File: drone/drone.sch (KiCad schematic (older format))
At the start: 16 parts

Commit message: Worked on the drone
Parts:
- X1: renamed from X?; value CRYSTAL -> 12MHz
- gave numbers to parts that had none: 15
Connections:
- no-connect marks 0 -> 9
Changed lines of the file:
@@
 $EndDescr
 $Comp
-L CRYSTAL X?
+L CRYSTAL X1
 U 1 1 556BC952
 P 1575 1875
-F 0 "X?" H 1575 2025 60  0000 C CNN
-F 1 "CRYSTAL" H 1575 1725 60  0000 C CNN
+F 0 "X1" H 1575 2025 60  0000 C CNN
+F 1 "12MHz" H 1575 1725 60  0000 C CNN
 F 2 "" H 1575 1875 60  0000 C CNN
 F 3 "" H 1575 1875 60  0000 C CNN
@@
 $EndComp
 $Comp
-L AT89S4051-P IC?
+L AT89S4051-P IC1
 U 1 1 556CD57A
 P 3125 2175
-F 0 "IC?" H 2175 3175 40  0000 C CNN
+F 0 "IC1" H 2175 3175 40  0000 C CNN
 F 1 "AT89S4051-P" H 3875 1275 40  0000 C CNN
 F 2 "DIP20" H 3125 2175 30  0000 C CIN
@@
 $EndComp
 $Comp
-L RELAY_2RT K?
+L RELAY_2RT K2
 U 1 1 556CD7C9
 P 9575 1125
-F 0 "K?" H 9525 1525 70  0000 C CNN
+F 0 "K2" H 9525 1525 70  0000 C CNN
 F 1 "RELAY_2RT" H 9725 625 70  0000 C CNN
 F 2 "" H 9575 1125 60  0000 C CNN
@@
 $EndComp
 $Comp
-L CONN_2 P?
+L CONN_2 P3
 U 1 1 556CD7F2
 P 8750 1025
-F 0 "P?" V 8700 1025 40  0000 C CNN
+F 0 "P3" V 8700 1025 40  0000 C CNN
 F 1 "CONN_2" V 8800 1025 40  0000 C CNN
 F 2 "" H 8750 1025 60  0000 C CNN
@@
 $EndComp
 $Comp
-L +12V #PWR?
+L +12V #PWR01
 U 1 1 556CD84C
 P 10150 775
-F 0 "#PWR?" H 10150 725 20  0001 C CNN
+F 0 "#PWR01" H 10150 725 20  0001 C CNN
 F 1 "+12V" H 10150 875 30  0000 C CNN
 F 2 "" H 10150 775 60  0000 C CNN
@@
 $EndComp
 $Comp
-L +12V #PWR?
+L +12V #PWR02
 U 1 1 556CD860
 P 10150 1275
-F 0 "#PWR?" H 10150 1225 20  0001 C CNN
+F 0 "#PWR02" H 10150 1225 20  0001 C CNN
 F 1 "+12V" H 10150 1375 30  0000 C CNN
 F 2 "" H 10150 1275 60  0000 C CNN
@@
 $EndComp
 $Comp
-L GND #PWR?
+L GND #PWR03
 U 1 1 556CD879
 P 10150 975
-F 0 "#PWR?" H 10150 975 30  0001 C CNN
+F 0 "#PWR03" H 10150 975 30  0001 C CNN
 F 1 "GND" H 10150 905 30  0001 C CNN
 F 2 "" H 10150 975 60  0000 C CNN
@@
 $EndComp
 $Comp
-L GND #PWR?
+L GND #PWR04
 U 1 1 556CD88D
 P 10150 1075
-F 0 "#PWR?" H 10150 1075 30  0001 C CNN
+F 0 "#PWR04" H 10150 1075 30  0001 C CNN
 F 1 "GND" H 10150 1005 30  0001 C CNN
 F 2 "" H 10150 1075 60  0000 C CNN
@@
 $EndComp
 $Comp
-L NPN Q?
+L NPN Q2
 U 1 1 556CDBB5
 P 8775 1475
-F 0 "Q?" H 8775 1325 50  0000 R CNN
+F 0 "Q2" H 8775 1325 50  0000 R CNN
 F 1 "NPN" H 8775 1625 50  0000 R CNN
 F 2 "" H 8775 1475 60  0000 C CNN
@@
 $EndComp
 $Comp
-L R R?
+L R R2
 U 1 1 556CDBC9
 P 8775 1975
-F 0 "R?" V 8855 1975 40  0000 C CNN
+F 0 "R2" V 8855 1975 40  0000 C CNN
 F 1 "3k3" V 8782 1976 40  0000 C CNN
 F 2 "" V 8705 1975 30  0000 C CNN
@@
 $EndComp
 $Comp
-L GND #PWR?
+L GND #PWR05
 U 1 1 556CDF27
 P 9150 1525
-F 0 "#PWR?" H 9150 1525 30  0001 C CNN
+F 0 "#PWR05" H 9150 1525 30  0001 C CNN
 F 1 "GND" H 9150 1455 30  0001 C CNN
 F 2 "" H 9150 1525 60  0000 C CNN
@@
 MotorRight
 $Comp
-L C C?
+L C C1
 U 1 1 556CE658
 P 1125 1575
-F 0 "C?" H 1125 1675 40  0000 L CNN
+F 0 "C1" H 1125 1675 40  0000 L CNN
 F 1 "5pF" H 1131 1490 40  0000 L CNN
 F 2 "" H 1163 1425 30  0000 C CNN
@@
 $EndComp
 $Comp
-L C C?
+L C C2
 U 1 1 556CE66C
 P 1125 2175
-F 0 "C?" H 1125 2275 40  0000 L CNN
+F 0 "C2" H 1125 2275 40  0000 L CNN
 F 1 "5pF" H 1131 2090 40  0000 L CNN
 F 2 "" H 1163 2025 30  0000 C CNN
@@
 $EndComp
 $Comp
-L GND #PWR?
+L GND #PWR06
 U 1 1 556CE6AB
 P 3125 3200
-F 0 "#PWR?" H 3125 3200 30  0001 C CNN
+F 0 "#PWR06" H 3125 3200 30  0001 C CNN
 F 1 "GND" H 3125 3130 30  0001 C CNN
 F 2 "" H 3125 3200 60  0000 C CNN
@@
 $EndComp
 $Comp
-L GND #PWR?
+L GND #PWR07
 U 1 1 556CE7FF
 P 925 2325
-F 0 "#PWR?" H 925 2325 30  0001 C CNN
+F 0 "#PWR07" H 925 2325 30  0001 C CNN
 F 1 "GND" H 925 2255 30  0001 C CNN
 F 2 "" H 925 2325 60  0000 C CNN
@@
 $EndComp
 $Comp
-L SW_PUSH_SMALL SW?
+L SW_PUSH_SMALL SW1
 U 1 1 556CEA9C
 P 1875 1150
-F 0 "SW?" H 2025 1260 30  0000 C CNN
+F 0 "SW1" H 2025 1260 30  0000 C CNN
 F 1 "SW_PUSH_SMALL" H 1875 1071 30  0000 C CNN
 F 2 "" H 1875 1150 60  0000 C CNN
@@
 $EndComp
 $Comp
-L +5V #PWR?
+L +5V #PWR08
 U 1 1 556CEAC9
 P 1775 1000
-F 0 "#PWR?" H 1775 1090 20  0001 C CNN
+F 0 "#PWR08" H 1775 1090 20  0001 C CNN
 F 1 "+5V" H 1775 1090 30  0000 C CNN
 F 2 "" H 1775 1000 60  0000 C CNN
@@
 $EndComp
 $Comp
-L +5V #PWR?
+L +5V #PWR09
 U 1 1 556D0B9E
 P 8550 1350
-F 0 "#PWR?" H 8550 1440 20  0001 C CNN
+F 0 "#PWR09" H 8550 1440 20  0001 C CNN
 F 1 "+5V" H 8550 1440 30  0000 C CNN
 F 2 "" H 8550 1350 60  0000 C CNN
@@
 Int0
 $Comp
-L SW_PUSH SW?
+L SW_PUSH SW3
 U 1 1 556E0334
 P 9600 3750
-F 0 "SW?" H 9750 3860 50  0000 C CNN
+F 0 "SW3" H 9750 3860 50  0000 C CNN
 F 1 "SW_PUSH" H 9600 3670 50  0000 C CNN
 F 2 "" H 9600 3750 60  0000 C CNN
@@
 Connection ~ 9200 3550
 $Comp
-L +5V #PWR?
+L +5V #PWR010
 U 1 1 556E058A
 P 9925 3225
-F 0 "#PWR?" H 9925 3315 20  0001 C CNN
+F 0 "#PWR010" H 9925 3315 20  0001 C CNN
 F 1 "+5V" H 9925 3315 30  0000 C CNN
 F 2 "" H 9925 3225 60  0000 C CNN
@@
 	9300 3425 9200 3425
 $Comp
-L SW_PUSH SW?
+L SW_PUSH SW2
 U 1 1 556E06D3
 P 9600 3425
-F 0 "SW?" H 9750 3535 50  0000 C CNN
+F 0 "SW2" H 9750 3535 50  0000 C CNN
 F 1 "SW_PUSH" H 9600 3345 50  0000 C CNN
 F 2 "" H 9600 3425 60  0000 C CNN
@@
 	9200 3750 9300 3750
 $Comp
-L +5V #PWR?
+L +5V #PWR011
 U 1 1 556E0901
 P 3125 1025
-F 0 "#PWR?" H 3125 1115 20  0001 C CNN
+F 0 "#PWR011" H 3125 1115 20  0001 C CNN
 F 1 "+5V" H 3125 1115 30  0000 C CNN
 F 2 "" H 3125 1025 60  0000 C CNN
@@
 	8775 2225 8775 2275
 $Comp
-L RELAY_2RT K?
+L RELAY_2RT K1
 U 1 1 556E1120
 P 7700 1225
-F 0 "K?" H 7650 1625 70  0000 C CNN
+F 0 "K1" H 7650 1625 70  0000 C CNN
 F 1 "RELAY_2RT" H 7850 725 70  0000 C CNN
 F 2 "" H 7700 1225 60  0000 C CNN
@@
 $EndComp
 $Comp
-L CONN_2 P?
+L CONN_2 P2
 U 1 1 556E1126
 P 6875 1125
-F 0 "P?" V 6825 1125 40  0000 C CNN
+F 0 "P2" V 6825 1125 40  0000 C CNN
 F 1 "CONN_2" V 6925 1125 40  0000 C CNN
 F 2 "" H 6875 1125 60  0000 C CNN
@@
 $EndComp
 $Comp
-L +12V #PWR?
+L +12V #PWR012
 U 1 1 556E112C
 P 8275 875
-F 0 "#PWR?" H 8275 825 20  0001 C CNN
+F 0 "#PWR012" H 8275 825 20  0001 C CNN
 F 1 "+12V" H 8275 975 30  0000 C CNN
 F 2 "" H 8275 875 60  0000 C CNN
@@
 $EndComp
 $Comp
-L +12V #PWR?
+L +12V #PWR013
 U 1 1 556E1132
 P 8275 1375
-F 0 "#PWR?" H 8275 1325 20  0001 C CNN
+F 0 "#PWR013" H 8275 1325 20  0001 C CNN
 F 1 "+12V" H 8275 1475 30  0000 C CNN
 F 2 "" H 8275 1375 60  0000 C CNN
@@
 $EndComp
 $Comp
-L GND #PWR?
+L GND #PWR014
 U 1 1 556E1138
 P 8275 1075
-F 0 "#PWR?" H 8275 1075 30  0001 C CNN
+F 0 "#PWR014" H 8275 1075 30  0001 C CNN
 F 1 "GND" H 8275 1005 30  0001 C CNN
 F 2 "" H 8275 1075 60  0000 C CNN
@@
 $EndComp
 $Comp
-L GND #PWR?
+L GND #PWR015
 U 1 1 556E113E
 P 8275 1175
-F 0 "#PWR?" H 8275 1175 30  0001 C CNN
+F 0 "#PWR015" H 8275 1175 30  0001 C CNN
 F 1 "GND" H 8275 1105 30  0001 C CNN
 F 2 "" H 8275 1175 60  0000 C CNN
@@
 $EndComp
 $Comp
-L NPN Q?
+L NPN Q1
 U 1 1 556E1144
 P 6900 1575
-F 0 "Q?" H 6900 1425 50  0000 R CNN
+F 0 "Q1" H 6900 1425 50  0000 R CNN
 F 1 "NPN" H 6900 1725 50  0000 R CNN
 F 2 "" H 6900 1575 60  0000 C CNN
@@
 $EndComp
 $Comp
-L R R?
+L R R1
 U 1 1 556E114A
 P 6900 2075
-F 0 "R?" V 6980 2075 40  0000 C CNN
+F 0 "R1" V 6980 2075 40  0000 C CNN
 F 1 "3k3" V 6907 2076 40  0000 C CNN
 F 2 "" V 6830 2075 30  0000 C CNN
@@
 $EndComp
 $Comp
-L GND #PWR?
+L GND #PWR016
 U 1 1 556E1150
 P 7275 1625
-F 0 "#PWR?" H 7275 1625 30  0001 C CNN
+F 0 "#PWR016" H 7275 1625 30  0001 C CNN
 F 1 "GND" H 7275 1555 30  0001 C CNN
 F 2 "" H 7275 1625 60  0000 C CNN
@@
 MotorLeft
 $Comp
-L +5V #PWR?
+L +5V #PWR017
 U 1 1 556E1157
 P 6675 1450
-F 0 "#PWR?" H 6675 1540 20  0001 C CNN
+F 0 "#PWR017" H 6675 1540 20  0001 C CNN
 F 1 "+5V" H 6675 1540 30  0000 C CNN
 F 2 "" H 6675 1450 60  0000 C CNN
@@
 Reset Button
 $Comp
-L CONN_3X2 P?
+L CONN_3X2 P1
 U 1 1 556E17F1
 P 5475 2025
-F 0 "P?" H 5475 2275 50  0000 C CNN
+F 0 "P1" H 5475 2275 50  0000 C CNN
 F 1 "CONN_3X2" V 5475 2075 40  0000 C CNN
 F 2 "" H 5475 2025 60  0000 C CNN
@@
 	1875 1375 1975 1375
 $Comp
-L GND #PWR?
+L GND #PWR018
 U 1 1 556E1AEE
 P 5875 2150
-F 0 "#PWR?" H 5875 2150 30  0001 C CNN
+F 0 "#PWR018" H 5875 2150 30  0001 C CNN
 F 1 "GND" H 5875 2080 30  0001 C CNN
 F 2 "" H 5875 2150 60  0000 C CNN
@@
 	5875 2150 5875 2075
 $Comp
-L +5V #PWR?
+L +5V #PWR019
 U 1 1 556E1B3C
 P 5875 1825
-F 0 "#PWR?" H 5875 1915 20  0001 C CNN
+F 0 "#PWR019" H 5875 1915 20  0001 C CNN
 F 1 "+5V" H 5875 1915 30  0000 C CNN
 F 2 "" H 5875 1825 60  0000 C CNN
@@
 Text Notes 9950 3925 2    60   ~ 0
 Bumper Switches
+NoConn ~ 4275 2675
+NoConn ~ 4275 2575
+NoConn ~ 4275 2375
+NoConn ~ 4275 2275
+NoConn ~ 4275 1775
+NoConn ~ 4275 1675
+NoConn ~ 4275 1575
+NoConn ~ 4275 1475
+NoConn ~ 4275 1375
 $EndSCHEMATC

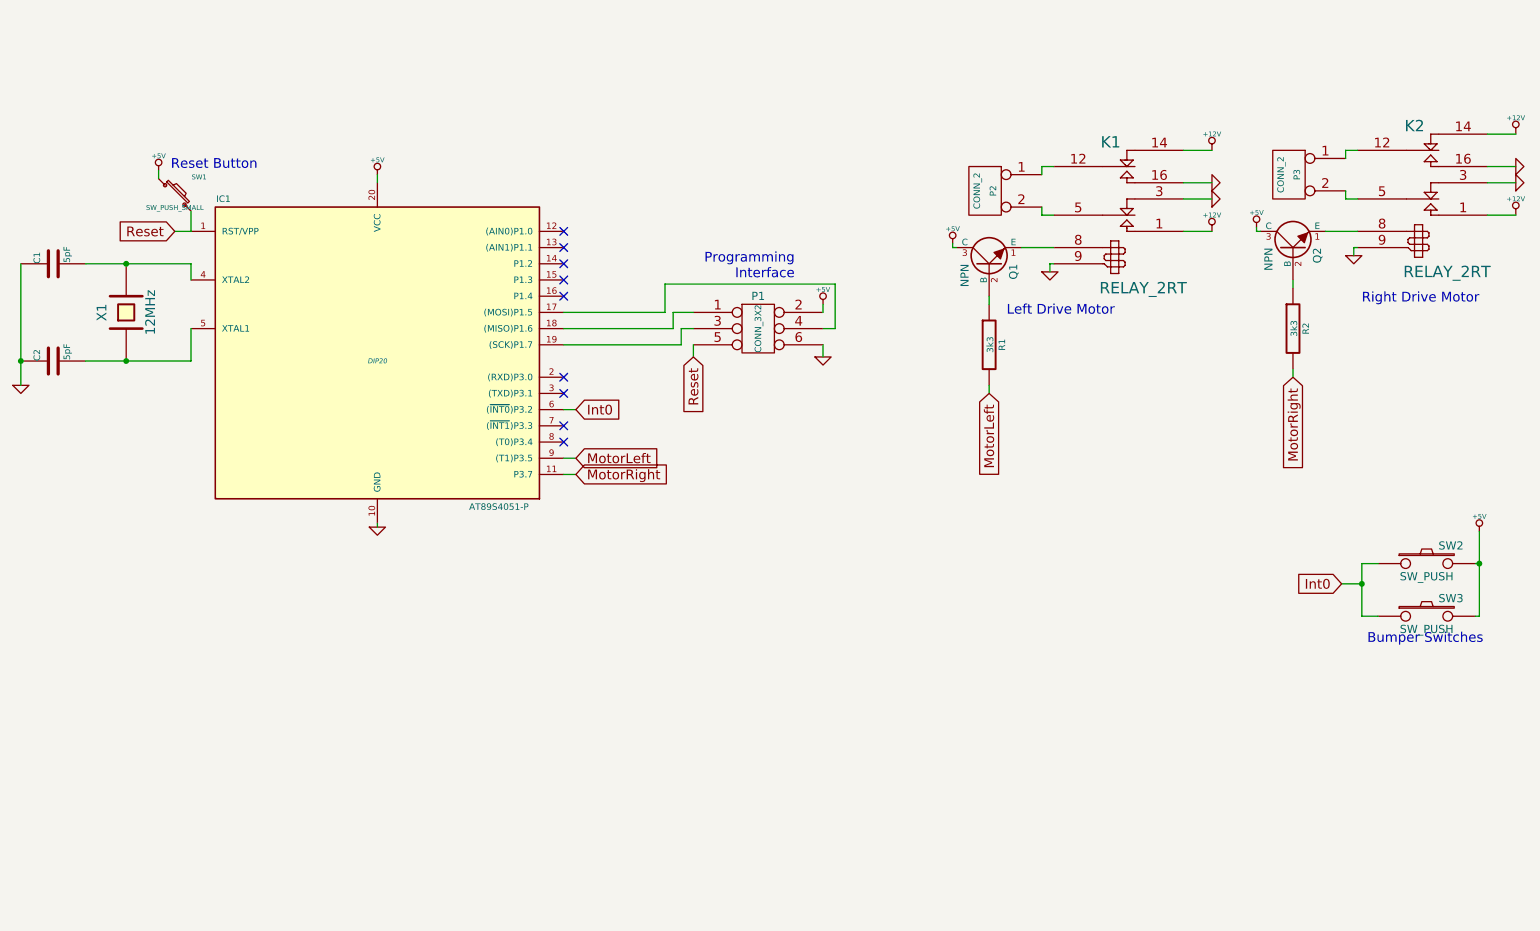
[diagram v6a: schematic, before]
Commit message: Added netlist
* Added the netlist
* Worked on the schematic
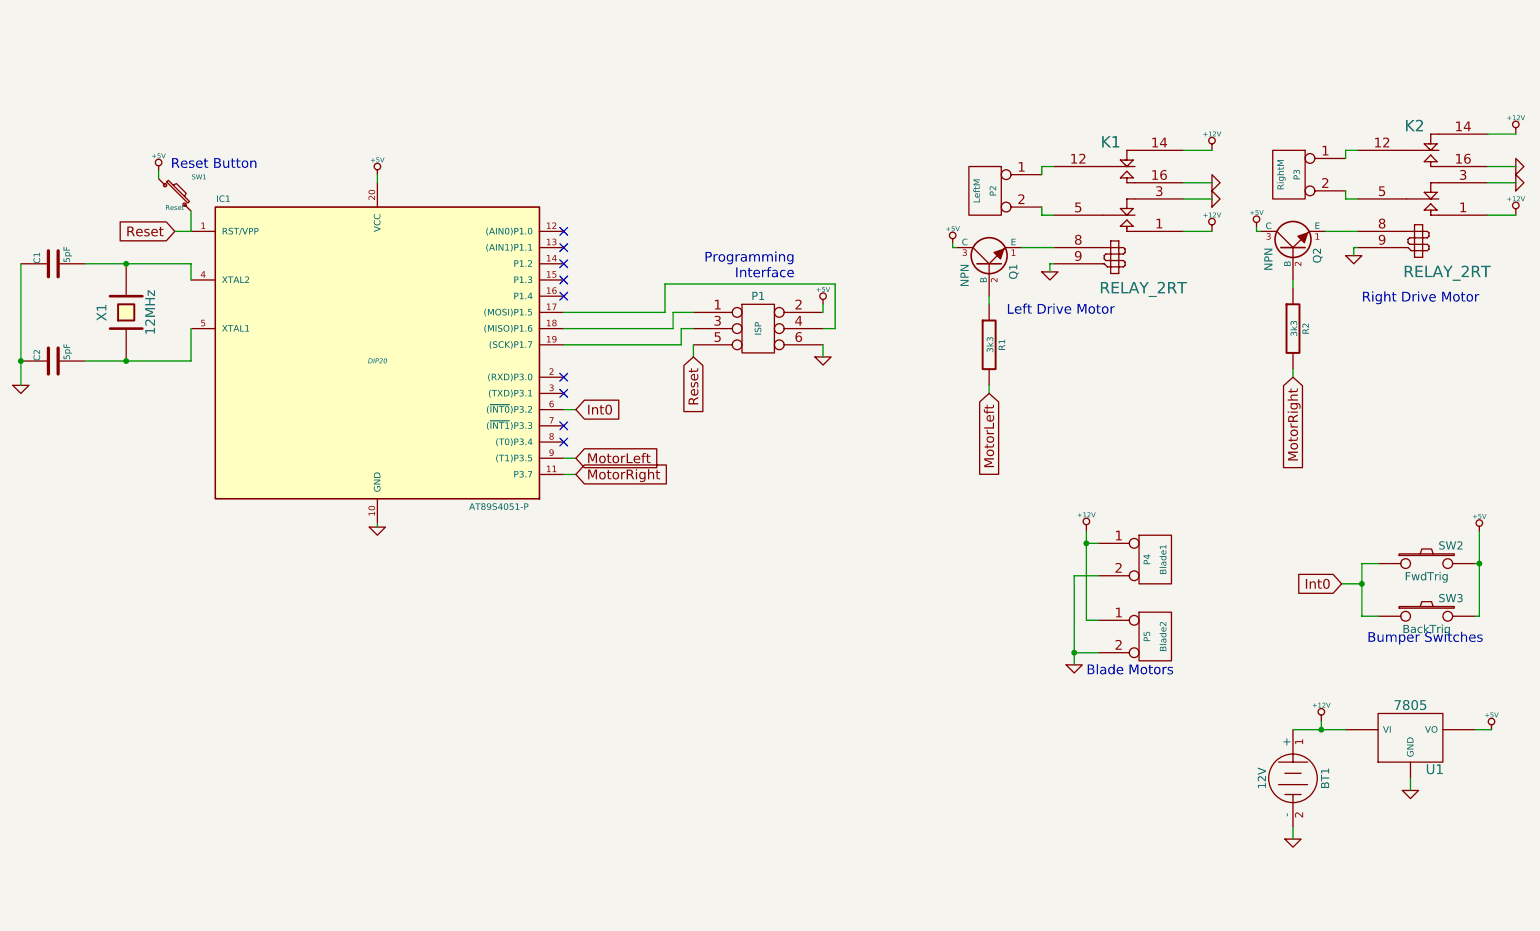
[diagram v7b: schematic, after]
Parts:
- added BT1: 12V, symbol BATTERY
- added P4: Blade1, symbol CONN_2
- added P5: Blade2, symbol CONN_2
- added U1: 7805, symbol 7805
- P1: value CONN_3X2 -> ISP
- P2: value CONN_2 -> LeftM
- P3: value CONN_2 -> RightM
- SW1: value SW_PUSH_SMALL -> Reset
- SW2: value SW_PUSH -> FwdTrig
- SW3: value SW_PUSH -> BackTrig
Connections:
- net +12V: now also BT1.1 (+), P4.1 (P1), P5.1 (P1), U1.VI
- net +5V: now also U1.VO
- net GND: now also BT1.2 (-), P4.2 (PM), P5.2 (PM), U1.GND
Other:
- note added: "Blade Motors"
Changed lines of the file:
@@
 P 8750 1025
 F 0 "P3" V 8700 1025 40  0000 C CNN
-F 1 "CONN_2" V 8800 1025 40  0000 C CNN
+F 1 "RightM" V 8800 1025 40  0000 C CNN
 F 2 "" H 8750 1025 60  0000 C CNN
 F 3 "" H 8750 1025 60  0000 C CNN
@@
 P 1875 1150
 F 0 "SW1" H 2025 1260 30  0000 C CNN
-F 1 "SW_PUSH_SMALL" H 1875 1071 30  0000 C CNN
+F 1 "Reset" H 1875 1071 30  0000 C CNN
 F 2 "" H 1875 1150 60  0000 C CNN
 F 3 "" H 1875 1150 60  0000 C CNN
@@
 P 9600 3750
 F 0 "SW3" H 9750 3860 50  0000 C CNN
-F 1 "SW_PUSH" H 9600 3670 50  0000 C CNN
+F 1 "BackTrig" H 9600 3670 50  0000 C CNN
 F 2 "" H 9600 3750 60  0000 C CNN
 F 3 "" H 9600 3750 60  0000 C CNN
@@
 P 9600 3425
 F 0 "SW2" H 9750 3535 50  0000 C CNN
-F 1 "SW_PUSH" H 9600 3345 50  0000 C CNN
+F 1 "FwdTrig" H 9600 3345 50  0000 C CNN
 F 2 "" H 9600 3425 60  0000 C CNN
 F 3 "" H 9600 3425 60  0000 C CNN
@@
 P 6875 1125
 F 0 "P2" V 6825 1125 40  0000 C CNN
-F 1 "CONN_2" V 6925 1125 40  0000 C CNN
+F 1 "LeftM" V 6925 1125 40  0000 C CNN
 F 2 "" H 6875 1125 60  0000 C CNN
 F 3 "" H 6875 1125 60  0000 C CNN
@@
 P 5475 2025
 F 0 "P1" H 5475 2275 50  0000 C CNN
-F 1 "CONN_3X2" V 5475 2075 40  0000 C CNN
+F 1 "ISP" V 5475 2075 40  0000 C CNN
 F 2 "" H 5475 2025 60  0000 C CNN
 F 3 "" H 5475 2025 60  0000 C CNN
@@
 NoConn ~ 4275 1475
 NoConn ~ 4275 1375
+$Comp
+L CONN_2 P4
+U 1 1 556F2AE8
+P 7925 3400
+F 0 "P4" V 7875 3400 40  0000 C CNN
+F 1 "Blade1" V 7975 3400 40  0000 C CNN
+F 2 "" H 7925 3400 60  0000 C CNN
+F 3 "" H 7925 3400 60  0000 C CNN
+	1    7925 3400
+	1    0    0    -1
+$EndComp
+$Comp
+L CONN_2 P5
+U 1 1 556F2AFC
+P 7925 3875
+F 0 "P5" V 7875 3875 40  0000 C CNN
+F 1 "Blade2" V 7975 3875 40  0000 C CNN
+F 2 "" H 7925 3875 60  0000 C CNN
+F 3 "" H 7925 3875 60  0000 C CNN
+	1    7925 3875
+	1    0    0    -1
+$EndComp
+$Comp
+L GND #PWR020
+U 1 1 556F2B21
+P 7425 4050
+F 0 "#PWR020" H 7425 4050 30  0001 C CNN
+F 1 "GND" H 7425 3980 30  0001 C CNN
+F 2 "" H 7425 4050 60  0000 C CNN
+F 3 "" H 7425 4050 60  0000 C CNN
+	1    7425 4050
+	1    0    0    -1
+$EndComp
+Wire Wire Line
+	7575 3500 7425 3500
+Wire Wire Line
+	7425 3500 7425 4050
+Wire Wire Line
+	7575 3975 7425 3975
+Connection ~ 7425 3975
+$Comp
+L +12V #PWR021
+U 1 1 556F2BC6
+P 7500 3225
+F 0 "#PWR021" H 7500 3175 20  0001 C CNN
+F 1 "+12V" H 7500 3325 30  0000 C CNN
+F 2 "" H 7500 3225 60  0000 C CNN
+F 3 "" H 7500 3225 60  0000 C CNN
+	1    7500 3225
+	1    0    0    -1
+$EndComp
+Wire Wire Line
+	7500 3225 7500 3775
+Wire Wire Line
+	7500 3300 7575 3300
+Wire Wire Line
+	7500 3775 7575 3775
+Connection ~ 7500 3300
+Text Notes 7500 4125 0    60   ~ 0
+Blade Motors
+$Comp
+L BATTERY BT1
+U 1 1 556F306E
+P 8775 4750
+F 0 "BT1" H 8775 4950 50  0000 C CNN
+F 1 "12V" H 8775 4560 50  0000 C CNN
+F 2 "" H 8775 4750 60  0000 C CNN
+F 3 "" H 8775 4750 60  0000 C CNN
+	1    8775 4750
+	0    1    1    0
+$EndComp
+$Comp
+L +12V #PWR022
+U 1 1 556F3087
+P 8950 4400
+F 0 "#PWR022" H 8950 4350 20  0001 C CNN
+F 1 "+12V" H 8950 4500 30  0000 C CNN
+F 2 "" H 8950 4400 60  0000 C CNN
+F 3 "" H 8950 4400 60  0000 C CNN
+	1    8950 4400
+	1    0    0    -1
+$EndComp
+$Comp
+L +5V #PWR023
+U 1 1 556F309B
+P 10000 4450
+F 0 "#PWR023" H 10000 4540 20  0001 C CNN
+F 1 "+5V" H 10000 4540 30  0000 C CNN
+F 2 "" H 10000 4450 60  0000 C CNN
+F 3 "" H 10000 4450 60  0000 C CNN
+	1    10000 4450
+	1    0    0    -1
+$EndComp
+$Comp
+L GND #PWR024
+U 1 1 556F30B9
+P 8775 5125
+F 0 "#PWR024" H 8775 5125 30  0001 C CNN
+F 1 "GND" H 8775 5055 30  0001 C CNN
+F 2 "" H 8775 5125 60  0000 C CNN
+F 3 "" H 8775 5125 60  0000 C CNN
+	1    8775 5125
+	1    0    0    -1
+$EndComp
+Wire Wire Line
+	8775 5125 8775 5050
+$Comp
+L 7805 U1
+U 1 1 556F311C
+P 9500 4500
+F 0 "U1" H 9650 4304 60  0000 C CNN
+F 1 "7805" H 9500 4700 60  0000 C CNN
+F 2 "" H 9500 4500 60  0000 C CNN
+F 3 "" H 9500 4500 60  0000 C CNN
+	1    9500 4500
+	1    0    0    -1
+$EndComp
+Wire Wire Line
+	8775 4450 9100 4450
+Wire Wire Line
+	8950 4450 8950 4400
+Connection ~ 8950 4450
+Wire Wire Line
+	9900 4450 10000 4450
+$Comp
+L GND #PWR025
+U 1 1 556F3243
+P 9500 4825
+F 0 "#PWR025" H 9500 4825 30  0001 C CNN
+F 1 "GND" H 9500 4755 30  0001 C CNN
+F 2 "" H 9500 4825 60  0000 C CNN
+F 3 "" H 9500 4825 60  0000 C CNN
+	1    9500 4825
+	1    0    0    -1
+$EndComp
+Wire Wire Line
+	9500 4825 9500 4750
 $EndSCHEMATC
